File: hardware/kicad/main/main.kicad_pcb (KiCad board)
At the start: 2 copper layers, 44.5 x 74 mm, 19 parts, among them J1 USB_C_Receptacle_USB2.0, J2 SERVO_L, J3 SERVO_R, J4 EXP_FRONT, J5 EXP_BACK, J6 ENC_LEFT, J7 ENC_RIGHT, U1 CH340G, U2 ESP32-WROOM-32, U3 ITR8307, U4 LM339, U5 IP5306

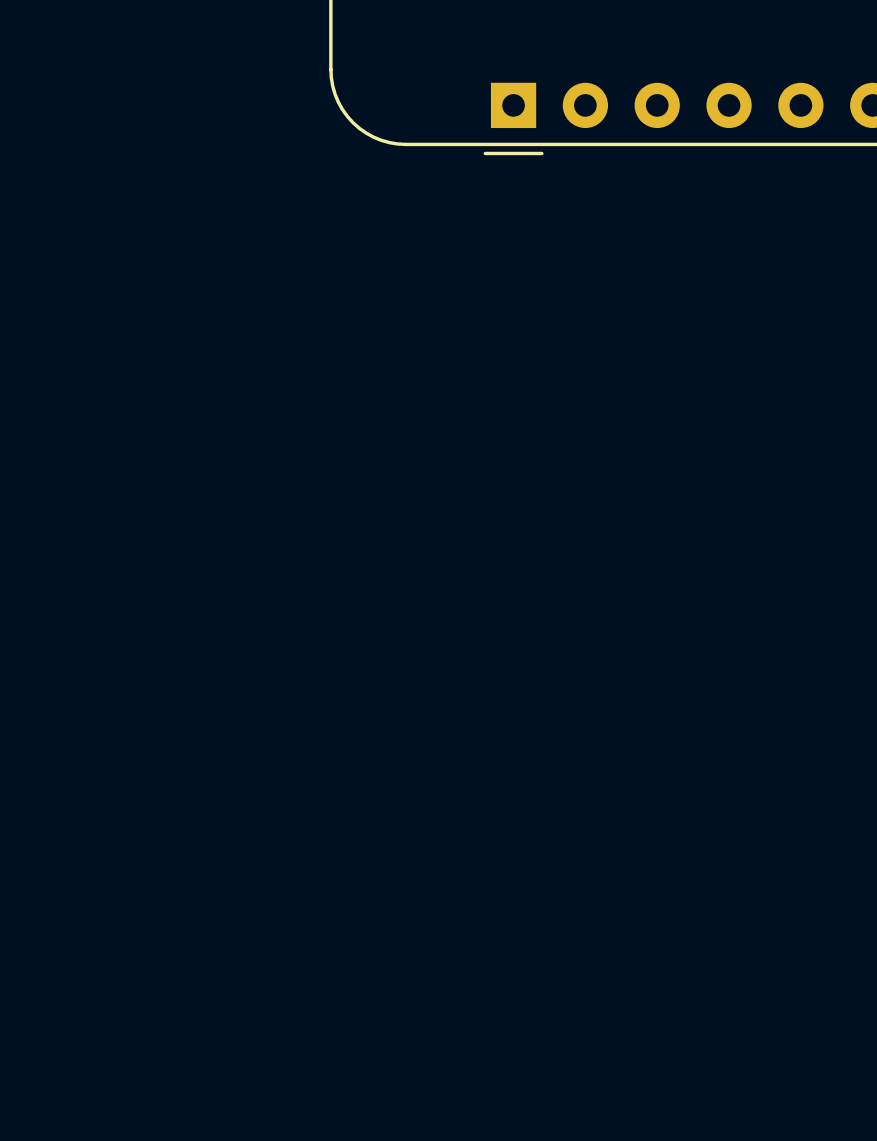
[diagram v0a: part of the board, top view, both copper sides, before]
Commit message: used espressif library
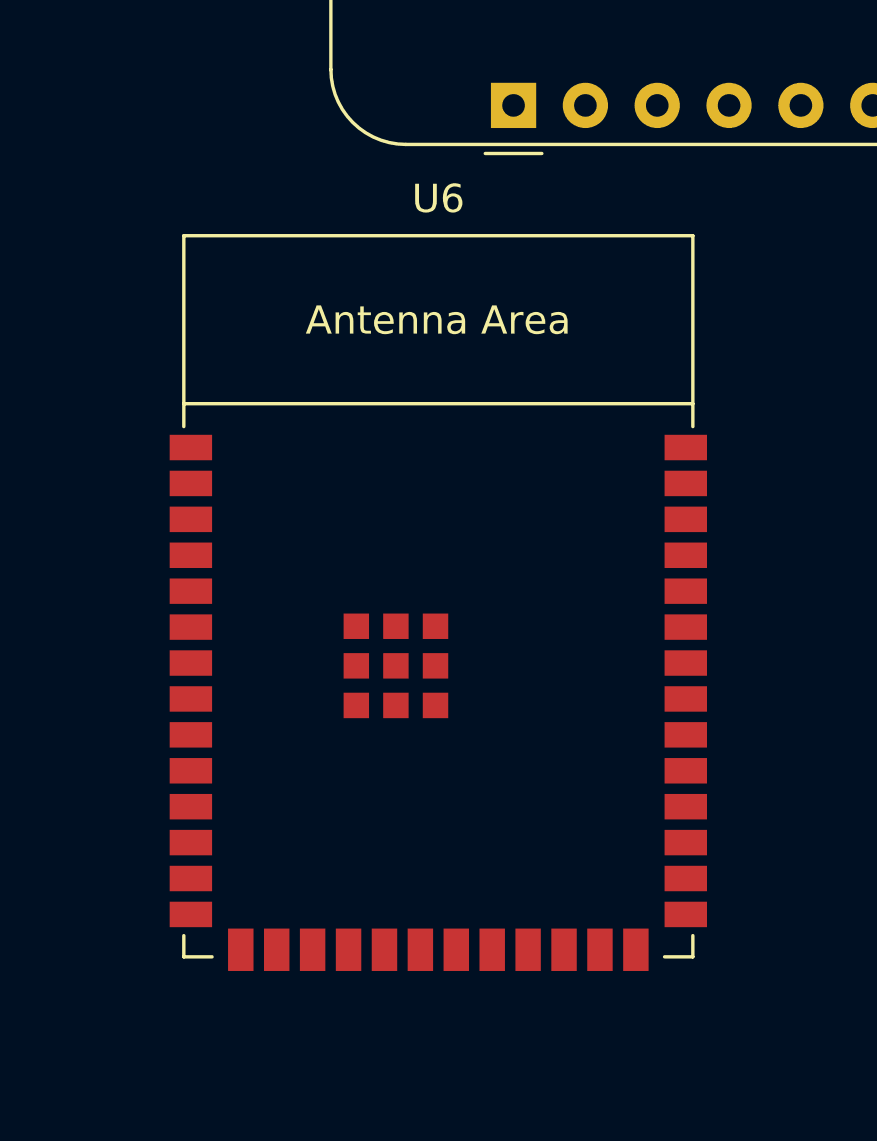
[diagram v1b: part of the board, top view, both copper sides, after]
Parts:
- added U6: ESP32-S3-WROOM-1, Espressif:ESP32-S3-WROOM-1, F.Cu at (184.3, 128.9)

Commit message: most of the routing done, left power supplies and navigation leds
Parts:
- added C1: 22u, Capacitor_SMD:C_1206_3216Metric, F.Cu at (115.5, 87.5)
- added C10: 100n, Capacitor_SMD:C_0603_1608Metric, F.Cu at (80.8, 87.9)
- added C11: 22u, Capacitor_SMD:C_1206_3216Metric, F.Cu at (110.0, 75.2)
- added C12: 100n, Capacitor_SMD:C_0603_1608Metric, F.Cu at (83.8, 113.0)
- added C13: 22u, Capacitor_SMD:C_1206_3216Metric, F.Cu at (80.8, 90.0)
- added C14: 22u, Capacitor_SMD:C_1206_3216Metric, F.Cu at (81.5, 119.5)
- added C15: 22u, Capacitor_SMD:C_1206_3216Metric, F.Cu at (115.5, 119.5)
- added C2: 22u, Capacitor_SMD:C_1206_3216Metric, F.Cu at (119.5, 87.5)
- added C3: 22u, Capacitor_SMD:C_1206_3216Metric, F.Cu at (105.2, 75.2)
- added C4: 22u, Capacitor_SMD:C_1206_3216Metric, F.Cu at (112.4, 80.0)
- added C5: 22u, Capacitor_SMD:C_1206_3216Metric, F.Cu at (110.0, 80.0)
- added C6: 22u, Capacitor_SMD:C_1206_3216Metric, F.Cu at (107.6, 80.0)
- added C7: 22u, Capacitor_SMD:C_1206_3216Metric, F.Cu at (105.2, 80.0)
- added C8: 22u, Capacitor_SMD:C_1206_3216Metric, F.Cu at (112.4, 75.2)
- added C9: 22u, Capacitor_SMD:C_1206_3216Metric, F.Cu at (107.6, 75.2)
- added D1: LESD5D5, Diode_SMD:D_SOD-523, F.Cu at (95.3, 118.0)
- added D2: LESD5D5, Diode_SMD:D_SOD-523, F.Cu at (98.7, 117.2)
- added D3: LESD5D5, Diode_SMD:D_SOD-523, F.Cu at (102.3, 117.2)
- added D4: W, LED_SMD:LED_0603_1608Metric, F.Cu at (95.3, 114.3)
- added D5: W, LED_SMD:LED_0603_1608Metric, F.Cu at (98.4, 115.0)
- added D6: W, LED_SMD:LED_0603_1608Metric, F.Cu at (101.6, 115.0)
- added D7: W, LED_SMD:LED_0603_1608Metric, F.Cu at (104.7, 114.3)
- added J10: ENC_LEFT, Connector_PinHeader_2.54mm:PinHeader_1x06_P2.54mm_Horizontal, F.Cu at (83.4, 106.3)
- added J11: ENC_RIGHT, Connector_PinHeader_2.54mm:PinHeader_1x06_P2.54mm_Horizontal, F.Cu at (116.6, 93.7)
- added J12: UART0, Connector_PinHeader_2.54mm:PinHeader_2x03_P2.54mm_Vertical, F.Cu at (102.9, 71.0)
- added J8: Conn_02x10_Odd_Even, Connector_PinSocket_2.54mm:PinSocket_2x10_P2.54mm_Vertical, B.Cu at (111.4, 62.1)
- added L1: L, Inductor_SMD:L_6.3x6.3_H3, F.Cu at (117.6, 81.6)
- added Q1: 2N7002K, Package_TO_SOT_SMD:SOT-23, F.Cu at (101.5, 81.0)
- added R1: 5k1, Resistor_SMD:R_0603_1608Metric, F.Cu at (97.7, 118.9)
- added R10: 10k, Resistor_SMD:R_0603_1608Metric, F.Cu at (102.5, 77.8)
- added R2: 5k1, Resistor_SMD:R_0603_1608Metric, F.Cu at (102.5, 118.9)
- added R3: 1R, Resistor_SMD:R_0603_1608Metric, F.Cu at (117.5, 86.8)
- added R4: 1R, Resistor_SMD:R_0603_1608Metric, F.Cu at (105.0, 83.2)
- added R5: 10k, Resistor_SMD:R_0603_1608Metric, F.Cu at (111.3, 88.4)
- added R6: 10k, Resistor_SMD:R_0603_1608Metric, F.Cu at (83.8, 109.8)
- added R7: 5k1, Resistor_SMD:R_0603_1608Metric, F.Cu at (115.8, 90.6)
- added R8: 10k, Resistor_SMD:R_0603_1608Metric, F.Cu at (119.2, 90.6)
- added SW1: SW_SPST, Button_Switch_SMD:SW_SPST_CK_RS282G05A3, F.Cu at (119.2, 112.2)
- added SW2: SW_SPST, Button_Switch_SMD:SW_SPST_CK_RS282G05A3, F.Cu at (80.8, 112.2)
- added SW3: SW_SPST, Button_Switch_SMD:SW_SPST_CK_RS282G05A3, F.Cu at (107.5, 121.4)
- added SW4: SW_SPST, Button_Switch_SMD:SW_SPST_CK_RS282G05A3, F.Cu at (92.5, 121.4)
- BT1: value Battery_Cell -> 18650
- U2: value ESP32-WROOM-32 -> AP1117-33; footprint RF_Module:ESP32-WROOM-32 -> Package_TO_SOT_SMD:SOT-223-3_TabPin2
- moved BT1 266.0 mm to (401.3, 104.0)
- moved A1 136.9 mm to (75.8, 188.5)
- moved U4 130.8 mm to (12.2, 4.61), turned to 0 degrees
- moved U1 123.5 mm to (3.73, 5.22), turned to 0 degrees
- moved U6 108.8 mm to (88.5, 77.3), turned to 90 degrees
- moved U3 86.3 mm to (195.6, 148.6)
- moved H2 70.1 mm to (118.0, 63.4)
- moved H1 70.1 mm to (82.0, 63.4)
- moved J5 63.1 mm to (172.7, 50.1)
- moved J1 60.0 mm to (100.0, 125.1), turned to 0 degrees
- moved J4 52.9 mm to (135.9, 160.7)
- moved H3 50.8 mm to (86.5, 116.5)
- moved U5 34.4 mm to (110.0, 85.1)
- moved J7 30.2 mm to (150.0, 94.9), turned to 0 degrees
- moved U2 29.7 mm to (117.4, 73.6)
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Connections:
- BT1 pad 1: unconnected-(BT1-+-Pad1) -> Net-(BT1-+)
- BT1 pad 2: unconnected-(BT1---Pad2) -> GND
- J1 pad A1: Net-(J1-GND-PadA1) -> GND
- J1 pad A12: Net-(J1-GND-PadA1) -> GND
- J1 pad A4: Net-(J1-VBUS-PadA4) -> +5VD
- J1 pad A5: unconnected-(J1-CC1-PadA5) -> Net-(J1-CC1)
- J1 pad A6: unconnected-(J1-D+-PadA6) -> /USB_D+
- J1 pad A7: unconnected-(J1-D--PadA7) -> /USB_D-
- J1 pad A8: unconnected-(J1-SBU1-PadA8) -> Net-(J1-SBU1)
- J1 pad A9: Net-(J1-VBUS-PadA4) -> +5VD
- J1 pad B1: Net-(J1-GND-PadA1) -> GND
- J1 pad B12: Net-(J1-GND-PadA1) -> GND
- J1 pad B4: Net-(J1-VBUS-PadA4) -> +5VD
- J1 pad B5: unconnected-(J1-CC2-PadB5) -> Net-(J1-CC2)
- J1 pad B6: unconnected-(J1-D+-PadB6) -> /USB_D+
- J1 pad B7: unconnected-(J1-D--PadB7) -> /USB_D-
- J1 pad B8: unconnected-(J1-SBU2-PadB8) -> Net-(J1-SBU1)
- J1 pad B9: Net-(J1-VBUS-PadA4) -> +5VD
- J1 pad S1: unconnected-(J1-SHIELD-PadS1) -> GND
- J2 pad 1: unconnected-(J2-Pin_1-Pad1) -> /GPIO15
- J2 pad 2: unconnected-(J2-Pin_2-Pad2) -> +5V
- J2 pad 3: unconnected-(J2-Pin_3-Pad3) -> GND
- J3 pad 1: unconnected-(J3-Pin_1-Pad1) -> /GPIO16
- J3 pad 2: unconnected-(J3-Pin_2-Pad2) -> +5V
- J3 pad 3: unconnected-(J3-Pin_3-Pad3) -> GND
- U2 pad 1: Net-(U2-GND-Pad1) -> GND
- U2 pad 2: unconnected-(U2-VDD-Pad2) -> +3.3V
- U2 pad 3: unconnected-(U2-EN-Pad3) -> +5V
- U5 pad 1: unconnected-(U5-VIN-Pad1) -> +5VD
- U5 pad 2: unconnected-(U5-LED1-Pad2) -> Net-(D4-A)
- U5 pad 3: unconnected-(U5-LED2-Pad3) -> Net-(D6-A)
- U5 pad 4: unconnected-(U5-LED3-Pad4) -> Net-(D4-K)
- U5 pad 5: unconnected-(U5-KEY-Pad5) -> Net-(U5-KEY)
- U5 pad 6: unconnected-(U5-BAT-Pad6) -> Net-(U5-BAT)
- U5 pad 7: unconnected-(U5-SW-Pad7) -> Net-(U5-SW)
- U5 pad 8: unconnected-(U5-VOUT-Pad8) -> +5V
- U5 pad 9: unconnected-(U5-GND-Pad9) -> GND
- U6 pad 1: Net-(U6-GND-Pad1) -> GND
- U6 pad 10: unconnected-(U6-GPIO17/U1TXD/ADC2_CH6-Pad10) -> /UART1_TX
- U6 pad 11: unconnected-(U6-GPIO18/U1RXD/ADC2_CH7/CLK_OUT3-Pad11) -> /UART1_RX
- U6 pad 12: unconnected-(U6-GPIO8/TOUCH8/ADC1_CH7/SUBSPICS1-Pad12) -> /GPIO8
- U6 pad 13: unconnected-(U6-GPIO19/U1RTS/ADC2_CH8/CLK_OUT2/USB_D--Pad13) -> /USB_D-
- U6 pad 14: unconnected-(U6-GPIO20/U1CTS/ADC2_CH9/CLK_OUT1/USB_D+-Pad14) -> /USB_D+
- U6 pad 15: unconnected-(U6-GPIO3/TOUCH3/ADC1_CH2-Pad15) -> /STRAP3
- U6 pad 16: unconnected-(U6-GPIO46-Pad16) -> /STRAP46
- U6 pad 17: unconnected-(U6-GPIO9/TOUCH9/ADC1_CH8/FSPIHD/SUBSPIHD-Pad17) -> /GPIO9/ADC1_8
- U6 pad 18: unconnected-(U6-GPIO10/TOUCH10/ADC1_CH9/FSPICS0/FSPIIO4/SUBSPICS0-Pad18) -> /GPIO10/ADC1_9
- U6 pad 19: unconnected-(U6-GPIO11/TOUCH11/ADC2_CH0/FSPID/FSPIIO5/SUBSPID-Pad19) -> /GPIO11
- U6 pad 2: unconnected-(U6-3V3-Pad2) -> +3.3V
- U6 pad 20: unconnected-(U6-GPIO12/TOUCH12/ADC2_CH1/FSPICLK/FSPIIO6/SUBSPICLK-Pad20) -> /GPIO12
- U6 pad 21: unconnected-(U6-GPIO13/TOUCH13/ADC2_CH2/FSPIQ/FSPIIO7/SUBSPIQ-Pad21) -> /GPIO13
- U6 pad 22: unconnected-(U6-GPIO14/TOUCH14/ADC2_CH3/FSPIWP/FSPIDQS/SUBSPIWP-Pad22) -> /GPIO14
- U6 pad 23: unconnected-(U6-GPIO21-Pad23) -> /GPIO21
- U6 pad 24: unconnected-(U6-GPIO47/SPICLK_P/SUBSPICLK_P_DIFF-Pad24) -> /GPIO47
- U6 pad 25: unconnected-(U6-GPIO48/SPICLK_N/SUBSPICLK_N_DIFF-Pad25) -> /GPIO48
- U6 pad 26: unconnected-(U6-GPIO45-Pad26) -> /STRAP45
- U6 pad 27: unconnected-(U6-GPIO0/BOOT-Pad27) -> /STRAP0
- U6 pad 28: unconnected-(U6-SPIIO6/GPIO35/FSPID/SUBSPID-Pad28) -> /PSRAM_35
- U6 pad 29: unconnected-(U6-SPIIO7/GPIO36/FSPICLK/SUBSPICLK-Pad29) -> /PSRAM_36
- U6 pad 3: unconnected-(U6-EN-Pad3) -> /~{RST}
- U6 pad 30: unconnected-(U6-SPIDQS/GPIO37/FSPIQ/SUBSPIQ-Pad30) -> /PSRAM_37
- U6 pad 31: unconnected-(U6-GPIO38/FSPIWP/SUBSPIWP-Pad31) -> /GPIO38
- U6 pad 32: unconnected-(U6-MTCK/GPIO39/CLK_OUT3/SUBSPICS1-Pad32) -> /GPIO39
- U6 pad 33: unconnected-(U6-MTDO/GPIO40/CLK_OUT2-Pad33) -> /GPIO40
- U6 pad 34: unconnected-(U6-MTDI/GPIO41/CLK_OUT1-Pad34) -> /GPIO41
- U6 pad 35: unconnected-(U6-MTMS/GPIO42-Pad35) -> /GPIO42
- U6 pad 36: unconnected-(U6-U0RXD/GPIO44/CLK_OUT2-Pad36) -> /UART0_RX
- U6 pad 37: unconnected-(U6-U0TXD/GPIO43/CLK_OUT1-Pad37) -> /UART0_TX
- U6 pad 38: unconnected-(U6-GPIO2/TOUCH2/ADC1_CH1-Pad38) -> /GPIO2/ADC1_1
- U6 pad 39: unconnected-(U6-GPIO1/TOUCH1/ADC1_CH0-Pad39) -> /GPIO1/ADC1_0
- U6 pad 4: unconnected-(U6-GPIO4/TOUCH4/ADC1_CH3-Pad4) -> /GPIO4
- U6 pad 40: Net-(U6-GND-Pad1) -> GND
- U6 pad 41: Net-(U6-GND-Pad1) -> GND
- U6 pad 5: unconnected-(U6-GPIO5/TOUCH5/ADC1_CH4-Pad5) -> /GPIO5
- U6 pad 6: unconnected-(U6-GPIO6/TOUCH6/ADC1_CH5-Pad6) -> /GPIO6
- U6 pad 7: unconnected-(U6-GPIO7/TOUCH7/ADC1_CH6-Pad7) -> /GPIO7/ADC1_6
- U6 pad 8: unconnected-(U6-GPIO15/U0RTS/ADC2_CH4/XTAL_32K_P-Pad8) -> /GPIO15
- U6 pad 9: unconnected-(U6-GPIO16/U0CTS/ADC2_CH5/XTAL_32K_N-Pad9) -> /GPIO16
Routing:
- net +5V: track 0.00 -> 138.7 mm, vias 0 -> 3
- net GND: track 0.00 -> 108.6 mm, vias 0 -> 5
- net +3.3V: track 0.00 -> 85.1 mm, vias 0 -> 2
- net +5VD: track 0.00 -> 83.3 mm
- net /GPIO16: track 0.00 -> 69.7 mm
- net /~{RST}: track 0.00 -> 64.2 mm, vias 0 -> 2
- net /STRAP0: track 0.00 -> 64.1 mm, vias 0 -> 3
- net /USB_D+: track 0.00 -> 55.9 mm, vias 0 -> 2
- net /USB_D-: track 0.00 -> 52.0 mm, vias 0 -> 2
- net Net-(D4-A): track 0.00 -> 49.9 mm, vias 0 -> 4
- net Net-(D4-K): track 0.00 -> 48.7 mm, vias 0 -> 2
- net Net-(D6-A): track 0.00 -> 44.7 mm, vias 0 -> 2
- net /GPIO15: track 0.00 -> 42.9 mm
- net /GPIO11: track 0.00 -> 42.8 mm, vias 0 -> 1
- net Net-(BT1-+): track 0.00 -> 42.2 mm
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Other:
- board size 44.5 x 74 mm -> 116 x 137.5 mm

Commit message: routing pretty much done, passing DRC
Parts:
- removed A1: Adafruit_Feather_Generic, Module:Adafruit_Feather
- removed BT1: 18650, Battery:BatteryHolder_MPD_BH-18650-PC2
- removed J5: EXP_BACK, Connector_PinSocket_2.54mm:PinSocket_1x10_P2.54mm_Horizontal
- removed J6: ENC_LEFT, Connector_PinSocket_2.54mm:PinSocket_1x04_P2.54mm_Horizontal
- removed J7: ENC_RIGHT, Connector_PinSocket_2.54mm:PinSocket_1x04_P2.54mm_Horizontal
- removed REF**: mg90s, mg90s
- removed REF**: mg90s_right, mg90s:mg90s_right
- removed U1: CH340G, Package_SO:SOIC-16_3.9x9.9mm_P1.27mm
- removed U3: ITR8307, OptoDevice:Everlight_ITR8307
- removed U4: LM339, Package_SO:SOIC-14_3.9x8.7mm_P1.27mm
- added D10: G, LED_SMD:LED_0603_1608Metric, F.Cu at (119.8, 125.5)
- added D11: B, LED_SMD:LED_0603_1608Metric, F.Cu at (100.0, 66.6)
- added D8: SK6812MINI, LED_SMD:LED_SK6812MINI_PLCC4_3.5x3.5mm_P1.75mm, F.Cu at (86.5, 89.5)
- added D9: R, LED_SMD:LED_0603_1608Metric, F.Cu at (80.2, 125.5)
- added H4: MountingHole_Pad, MountingHole:MountingHole_3.2mm_M3_DIN965_Pad, F.Cu at (113.0, 115.5)
- added R11: 1k, Resistor_SMD:R_0603_1608Metric, F.Cu at (116.5, 125.5)
- added R12: 1k, Resistor_SMD:R_0603_1608Metric, F.Cu at (96.8, 66.6)
- added R9: 1k, Resistor_SMD:R_0603_1608Metric, F.Cu at (83.5, 125.5)
- J10, J11, J12, J2, J3: moved to B.Cu
- J4: value EXP_FRONT -> Conn_01x02_Pin; footprint Connector_PinSocket_2.54mm:PinSocket_1x10_P2.54mm_Horizontal -> Connector_PinHeader_2.54mm:PinHeader_1x02_P2.54mm_Horizontal; moved to B.Cu
- moved J4 95.2 mm to (111.8, 68.6), turned to -90 degrees
- moved R5 19.1 mm to (119.2, 105.8), turned to -90 degrees
- moved J10 12.7 mm to (83.4, 93.7)
- moved J11 12.7 mm to (116.6, 106.3)
- moved J2 5.08 mm to (80.4, 122.6)
- moved J3 5.08 mm to (114.4, 122.6)
- moved J12 5.05 mm to (108.0, 71.1)
- moved C14 1.50 mm to (83.0, 119.5)
- moved C15 1.50 mm to (117.0, 119.5)
- moved H3 1.12 mm to (87.0, 115.5)
- moved C12 1.00 mm to (83.8, 112.0)
- moved R6 0.83 mm to (83.8, 109.0)
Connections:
- C2 pad 1: Net-(BT1-+) -> Net-(J4-Pin_2)
- H1 pad 1: unconnected-(H1-Pad1) -> GND
- H2 pad 1: unconnected-(H2-Pad1) -> GND
- H3 pad 1: unconnected-(H3-Pad1) -> GND
- J10 pad 1: GND -> /GPIO6
- J10 pad 2: +3.3V -> /STRAP45
- J10 pad 3: /GPIO4 -> /GPIO5
- J10 pad 4: /GPIO5 -> /GPIO4
- J10 pad 5: /STRAP45 -> +3.3V
- J10 pad 6: /GPIO6 -> GND
- J11 pad 1: GND -> /STRAP3
- J11 pad 2: +3.3V -> /STRAP46
- J11 pad 5: /STRAP46 -> +3.3V
- J11 pad 6: /STRAP3 -> GND
- J12 pad 1: /UART0_TX -> GND
- J12 pad 2: /STRAP0 -> +3.3V
- J12 pad 5: GND -> /UART0_TX
- J12 pad 6: +3.3V -> /STRAP0
- J2 pad 1: /GPIO15 -> GND
- J2 pad 3: GND -> /GPIO15
- J3 pad 1: /GPIO16 -> GND
- J3 pad 3: GND -> /GPIO16
- J4 pad 1: unconnected-(J4-Pin_1-Pad1) -> GND
- J4 pad 2: unconnected-(J4-Pin_2-Pad2) -> Net-(J4-Pin_2)
- L1 pad 2: Net-(BT1-+) -> Net-(J4-Pin_2)
- R3 pad 1: Net-(BT1-+) -> Net-(J4-Pin_2)
- R7 pad 2: Net-(BT1-+) -> Net-(J4-Pin_2)
- SW3 pad 1: unconnected-(SW3-A-Pad1) -> GND
- SW3 pad 2: unconnected-(SW3-B-Pad2) -> /GPIO42
- SW4 pad 1: unconnected-(SW4-A-Pad1) -> GND
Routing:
- net GND: track 108.6 -> 350.4 mm, vias 5 -> 120
- net +3.3V: track 85.1 -> 206.8 mm, vias 2 -> 10
- net /GPIO40: track 5.64 -> 114.8 mm, vias 0 -> 5
- net /GPIO42: track 5.79 -> 90.4 mm, vias 0 -> 2
- net Net-(BT1-+): track 42.2 -> 0.00 mm
- net Net-(J4-Pin_2): track 0.00 -> 41.0 mm, vias 0 -> 3
- net Net-(SW1-A): track 29.6 -> 1.77 mm, vias 2 -> 0
- net /~{RST}: track 64.2 -> 87.0 mm, vias 2 -> 4
- net Net-(U5-KEY): track 1.52 -> 21.9 mm, vias 0 -> 2
- net /GPIO41: track 5.58 -> 25.7 mm, vias 0 -> 2
- net +5VD: track 83.3 -> 72.7 mm
- net +5V: track 138.7 -> 128.6 mm, vias 3 -> 1
- net /UART0_TX: track 34.5 -> 29.2 mm
- net /UART0_RX: track 36.9 -> 31.8 mm
- net /GPIO4: track 17.1 -> 21.6 mm
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- added copper zone on B.Cu, net +3.3V
- added copper zone on B.Cu, net GND
- added copper zone on F.Cu, net GND
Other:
- outline, holes or cut-outs redrawn
- board text added: "3V3"
- board text added: "5V"
- board text added: "BAT+"
- board text added: "BAT-"
- board text added: "G10A9"
- board text added: "G11"
- board text added: "G12"
- board text added: "G13"
- board text added: "G14"
- board text added: "G15"
- board text added: "G16"
- board text added: "G17TX1"
- board text added: "G18RX1"
- board text added: "G1A0"
- board text added: "G21"
- board text added: "G2A1"
- board text added: "G38"
- board text added: "G39"
- board text added: "G4"
- board text added: "G40"
- board text added: "G41"
- board text added: "G43TX0"
- board text added: "G44RX0"
- board text added: "G47"
- board text added: "G48"
- board text added: "G5"
- board text added: "G6"
- board text added: "G8"
- board text added: "G9A8"
- board text added: "GND"
- board text added: "NC"
- board text added: "RST"
- board text added: "S0"
- board text added: "S3"
- board text added: "S46"
